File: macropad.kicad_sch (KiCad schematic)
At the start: 26 parts, among them J1 SWD, Q1 PNP, SW10 Reset, SW11 Reset, U1 AP62250WU, U2 STM32F042K6Tx

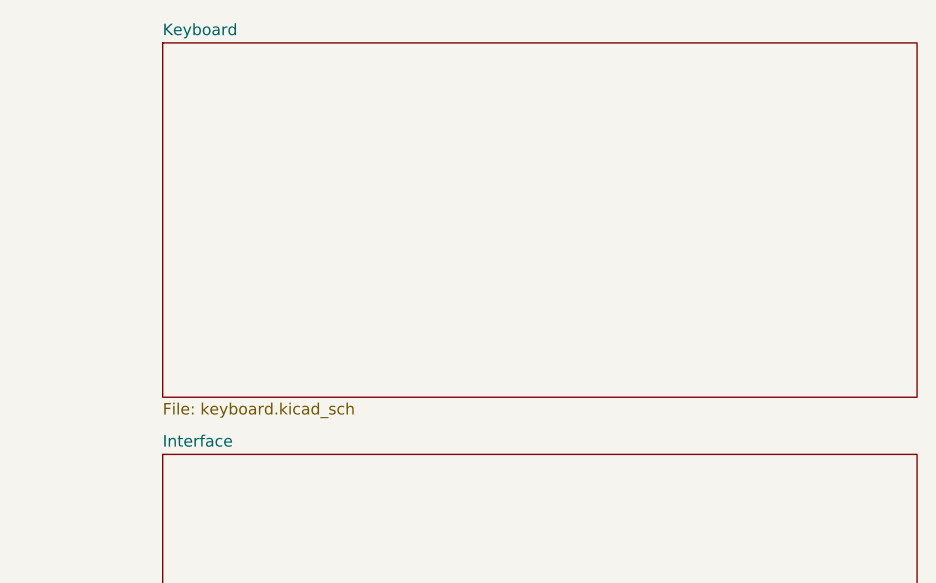
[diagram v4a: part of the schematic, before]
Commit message: Separated Keyboard schematic and pcb to a separate project in the same folder.
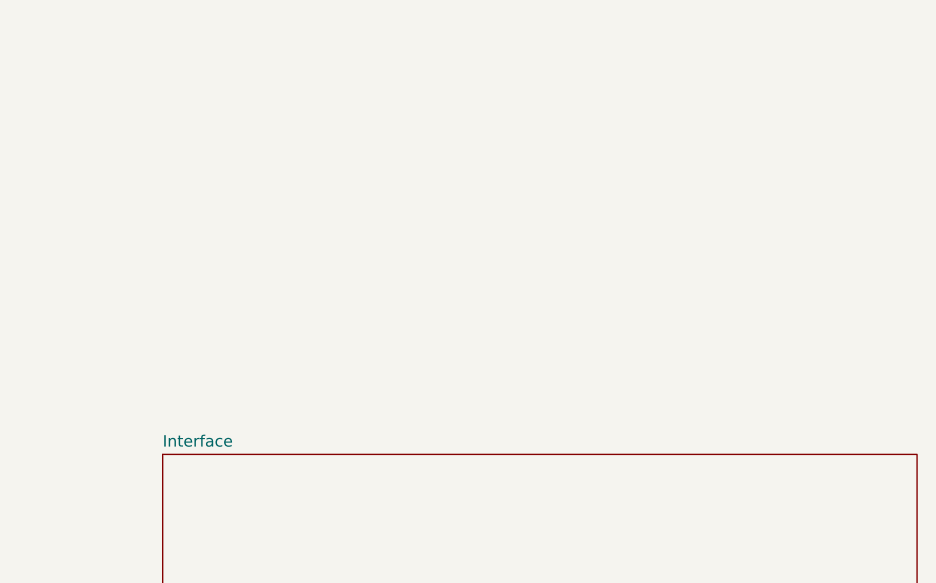
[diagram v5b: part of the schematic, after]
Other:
- removed sheet Keyboard
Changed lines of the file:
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@@
-		)
-	)
-	(sheet
-		(at 303.53 0)
-		(size 83.82 39.37)
-		(exclude_from_sim no)
-		(in_bom yes)
-		(on_board yes)
-		(dnp no)
-		(fields_autoplaced yes)
-		(stroke
-			(width 0.1524)
-			(type solid)
-		)
-		(fill
-			(color 0 0 0 0.0000)
-		)
-		(property "Sheetname" "Keyboard"
-			(at 303.53 -0.7116 0)
-			(effects
-				(font
-					(size 1.27 1.27)
-				)
-				(justify left bottom)
-			)
-		)
-		(property "Sheetfile" "keyboard.kicad_sch"
-			(at 303.53 39.9546 0)
-			(effects
-				(font
-					(size 1.27 1.27)
-				)
-				(justify left top)
-			)
-		)
-		(instances
-			(project "macropad"
-				(path "/affdcae3-2b9b-4248-bf2d-36ec8abc82bb"
-					(page "2")
-				)
-			)
 		)
 	)
